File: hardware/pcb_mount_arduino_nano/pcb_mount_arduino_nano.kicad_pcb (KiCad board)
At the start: 2 copper layers, 1 part

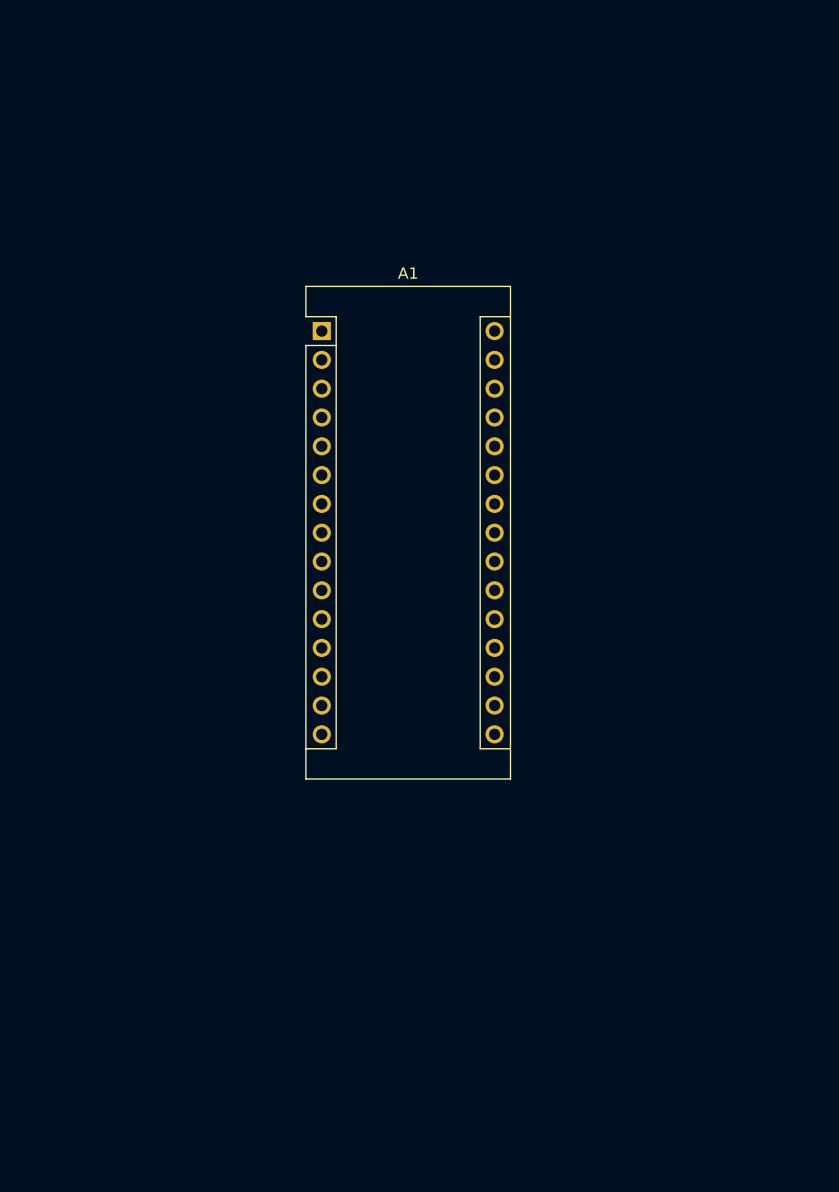
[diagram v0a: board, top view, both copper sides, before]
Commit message: Add mounting holes and DS18B20
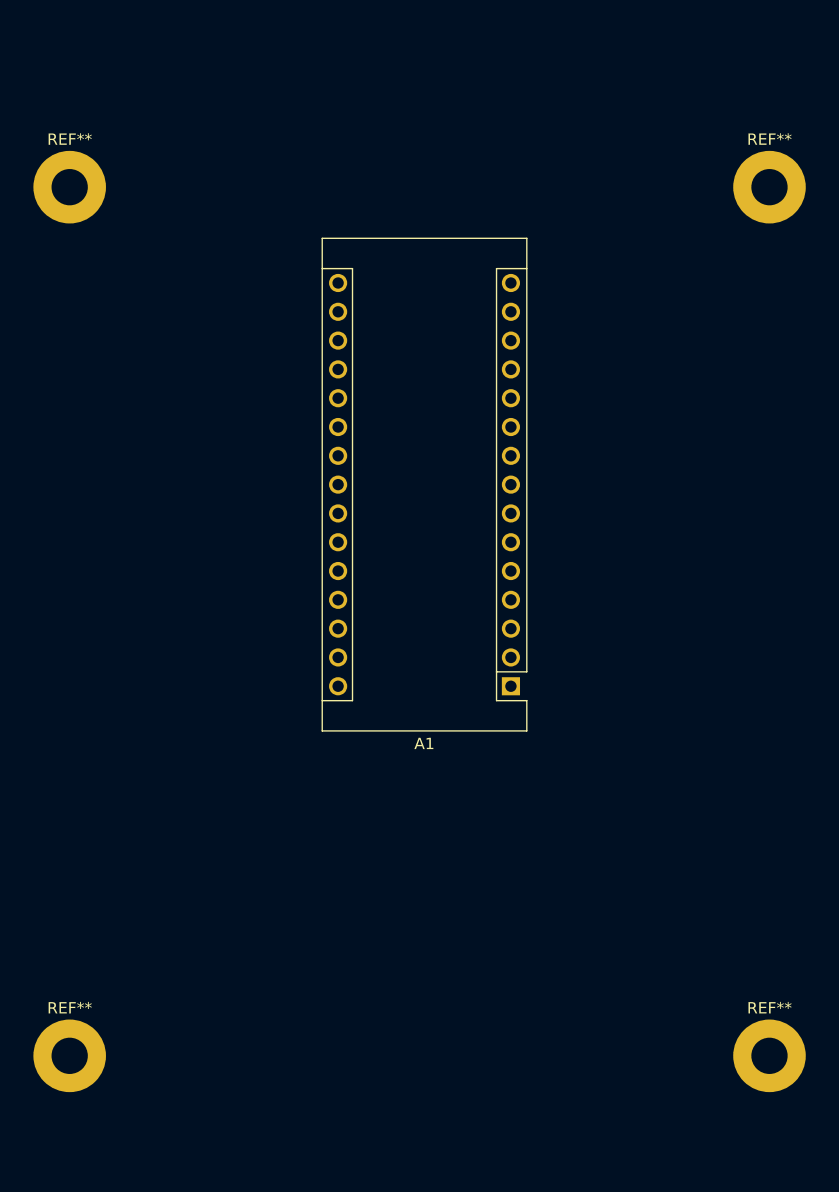
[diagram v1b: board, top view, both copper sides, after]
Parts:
- added REF**: MountingHole_3.2mm_M3_Pad, MountingHole:MountingHole_3.2mm_M3_Pad, F.Cu at (105.8, 120.6)
- added REF**: MountingHole_3.2mm_M3_Pad, MountingHole:MountingHole_3.2mm_M3_Pad, F.Cu at (44.1, 120.6)
- added REF**: MountingHole_3.2mm_M3_Pad, MountingHole:MountingHole_3.2mm_M3_Pad, F.Cu at (105.8, 44.0)
- added REF**: MountingHole_3.2mm_M3_Pad, MountingHole:MountingHole_3.2mm_M3_Pad, F.Cu at (44.1, 44.0)
- moved A1 35.5 mm to (83.0, 88.0), turned to 180 degrees

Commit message: Add serial port and power connector
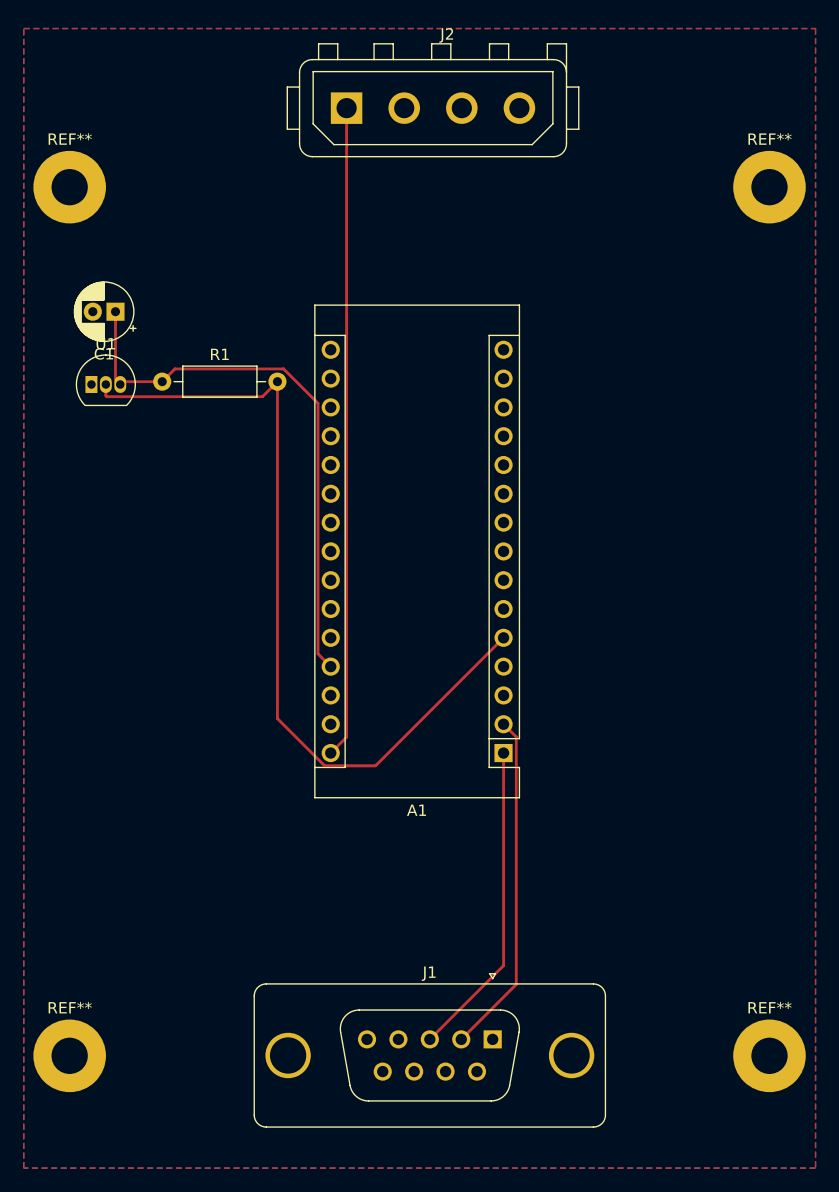
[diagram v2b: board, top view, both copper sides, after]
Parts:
- added C1: 10uF, Capacitor_THT:CP_Radial_D5.0mm_P2.00mm, F.Cu at (48.1, 55.0)
- added J1: DB9_Female_MountingHoles, Connector_Dsub:DSUB-9_Female_Vertical_P2.77x2.84mm_MountingHoles, F.Cu at (81.4, 119.2)
- added J2: Conn_01x04_Male, Connector_TE-Connectivity:TE_MATE-N-LOK_350211-1_1x04_P5.08mm_Vertical, F.Cu at (68.5, 37.0)
- added R1: 4k7, Resistor_THT:R_Axial_DIN0207_L6.3mm_D2.5mm_P10.16mm_Horizontal, F.Cu at (52.2, 61.1)
- added U1: DS18B20, Package_TO_SOT_THT:TO-92_Inline, F.Cu at (46.0, 61.4)
- moved A1 5.93 mm to (82.3, 93.9)
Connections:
- A1 pad 27: Net-(A1-Pad27) -> /+5v(REG)
- A1 pad 29: Net-(A1-Pad29) -> GND
- A1 pad 30: Net-(A1-Pad30) -> /+12v(IN)
- A1 pad 4: Net-(A1-Pad4) -> GND
- A1 pad 5: Net-(A1-Pad5) -> /1_WIRE
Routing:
- net /1_WIRE: track 0.00 -> 72.8 mm
- net /+12v(IN): track 0.00 -> 57.4 mm
- net /+5v(REG): track 0.00 -> 49.5 mm
- net Net-(A1-Pad2): track 0.00 -> 30.3 mm
- net Net-(A1-Pad1): track 0.00 -> 27.9 mm
- added copper zone on B.Cu, net GND
- added copper zone on F.Cu, net GND

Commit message: Convert graphic to edge cut
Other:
- board outline added: 69.8 x 100.5 mm

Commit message: Add multiple 1 wire temperature sensors
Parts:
- added U2: DS18B20, Package_TO_SOT_THT:TO-92_Inline, F.Cu at (45.9, 71.2)
- added U3: DS18B20, Package_TO_SOT_THT:TO-92_Inline, F.Cu at (45.9, 79.4)
- moved R1 39.8 mm to (48.4, 100.7)
- moved C1 31.3 mm to (47.7, 86.2)
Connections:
- net Net-(A1-Pad1) renamed /TX
- net Net-(A1-Pad2) renamed /RX
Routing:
- net /1_WIRE: track 72.8 -> 84.9 mm
- net /+5v(REG): track 49.5 -> 59.3 mm
